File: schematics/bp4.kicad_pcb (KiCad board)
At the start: 2 copper layers, 90 x 32.6 mm, 39 parts, among them J1 Left Pin Strip, J2 Right Pin Strip, J3 I/O Pin Strip, J4 Power Pins A, J5 Power Pins B, J6 Power Pins C, SW1 Power Switch, U1 TPS61220DCK, U2 LM321

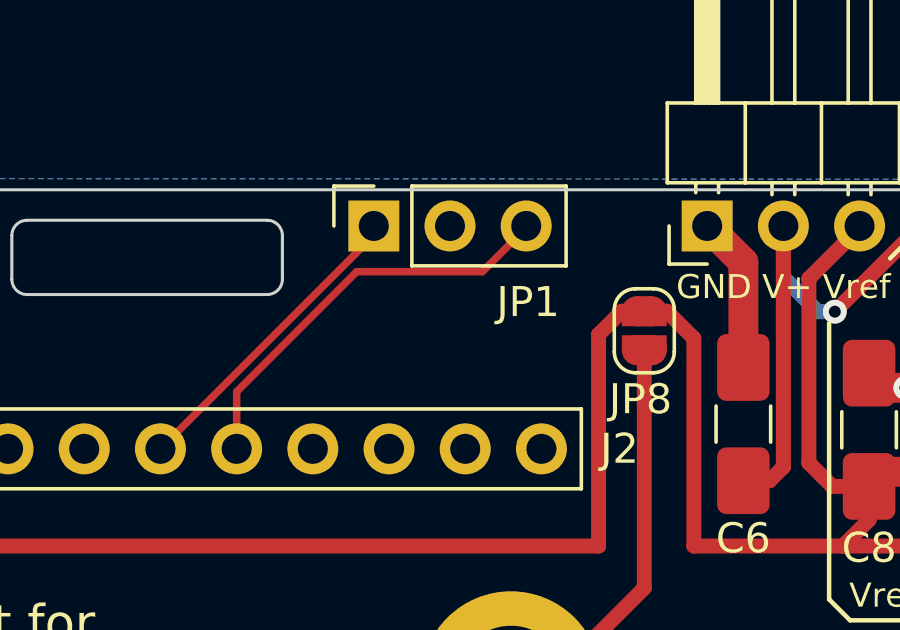
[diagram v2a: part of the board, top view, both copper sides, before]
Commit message: add silkscreen to JP1 pins
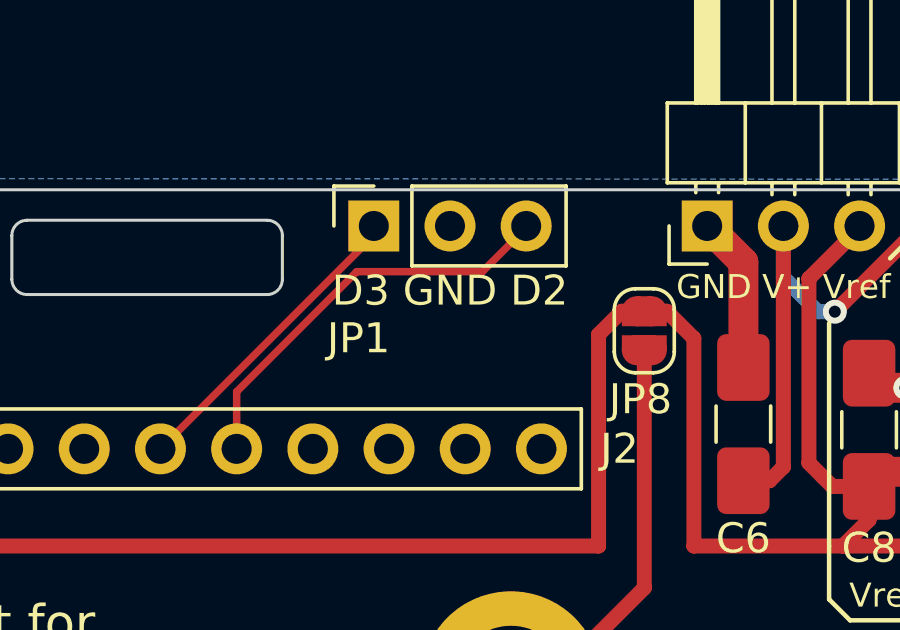
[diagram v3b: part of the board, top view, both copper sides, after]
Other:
- board text added: "D3 GND D2"
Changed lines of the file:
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@@
   (general
     (thickness 1.6)
-    (drawings 91)
+    (drawings 92)
     (tracks 306)
     (zones 0)
@@
     (descr "Through hole straight socket strip, 1x03, 2.54mm pitch, single row (from Kicad 4.0.7), script generated")
     (tags "Through hole socket strip THT 1x03 2.54mm single row")
-    (fp_text reference JP1 (at -2.54 5.1435 180) (layer F.SilkS)
+    (fp_text reference JP1 (at -3.7465 -0.508 180) (layer F.SilkS)
       (effects (font (size 1 1) (thickness 0.15)))
     )
@@
       (net 42 "Net-(JP8-Pad2)"))
   )
+  (gr_text "D3 GND D2" (at 59.309 28.7655) (layer F.SilkS)
+    (effects (font (size 1 1) (thickness 0.15)))
+  )
   (gr_line (start 108.2675 24.0665) (end 103.1875 30.7975) (layer Cmts.User) (width 0.15))

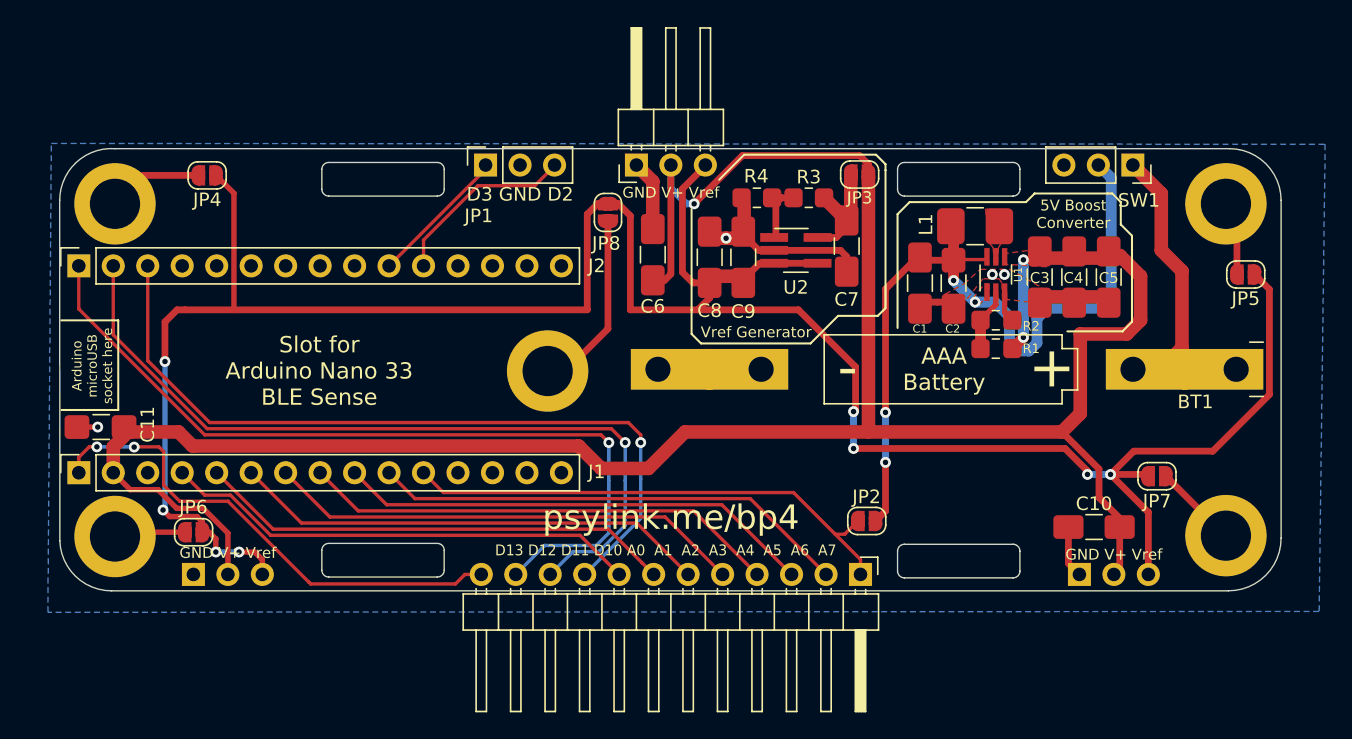
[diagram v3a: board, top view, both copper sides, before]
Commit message: swap horizontal pin headers for vertical pin headers
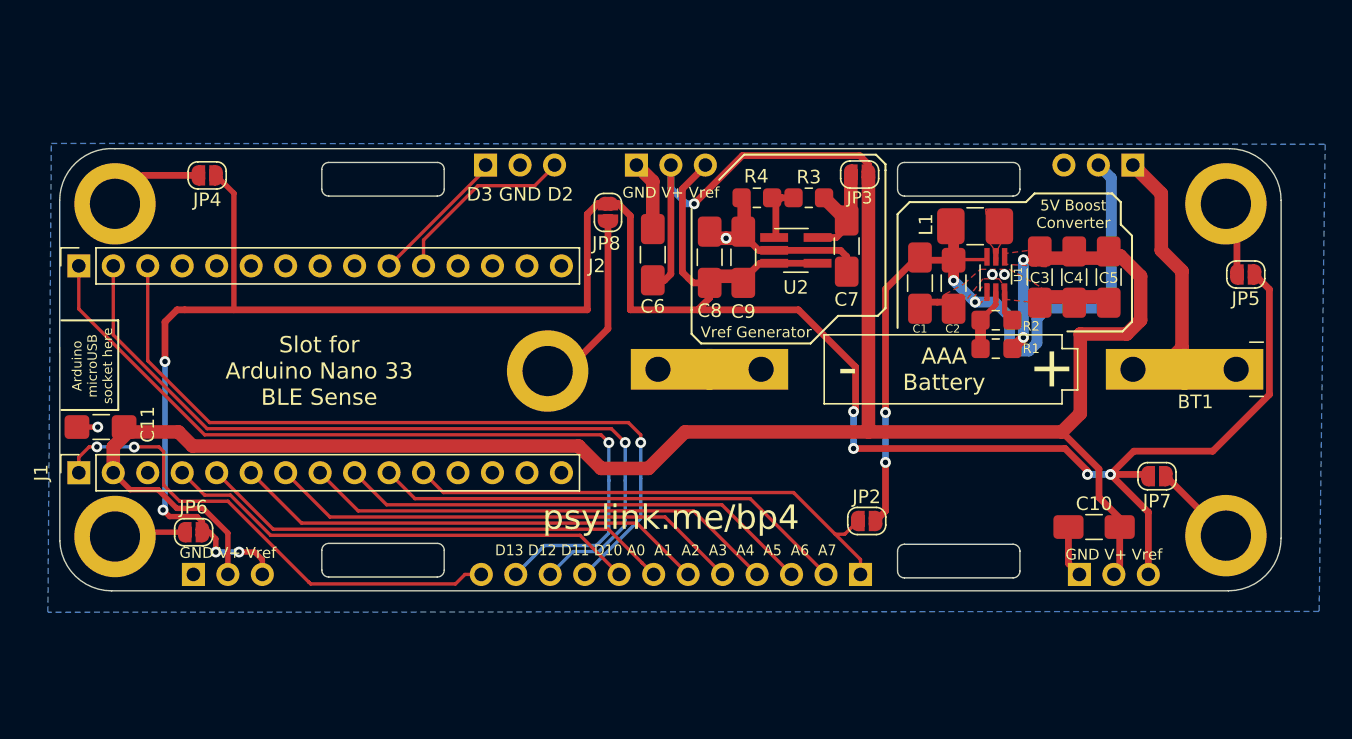
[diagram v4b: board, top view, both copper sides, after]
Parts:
- J3: footprint Connector_PinHeader_2.54mm:PinHeader_1x12_P2.54mm_Horizontal -> Connector_PinHeader_2.54mm:PinHeader_1x12_P2.54mm_Vertical; moved to B.Cu
- J4, J5: footprint Connector_PinHeader_2.54mm:PinHeader_1x03_P2.54mm_Horizontal -> Connector_PinHeader_2.54mm:PinHeader_1x03_P2.54mm_Vertical
- J6: footprint Connector_PinHeader_2.54mm:PinHeader_1x03_P2.54mm_Horizontal -> Connector_PinHeader_2.54mm:PinHeader_1x03_P2.54mm_Vertical; moved to B.Cu
- JP1, SW1: moved to B.Cu
- turned J3 to 90 degrees
- turned J6 to 270 degrees
- turned JP1 to 270 degrees
- turned SW1 to 90 degrees
